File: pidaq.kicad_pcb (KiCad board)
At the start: 2 copper layers, 83.8 x 78.1 mm, 39 parts, among them J1 Screw_Terminal_01x08, J2 Screw_Terminal_01x08, J3 Screw_Terminal_01x10, J4 Screw_Terminal_01x10, J5 Conn_01x02_Male, J6 Conn_01x08_Female, U1 LTC2984CLX-PBF, U2 LTC2418IGN-PBF

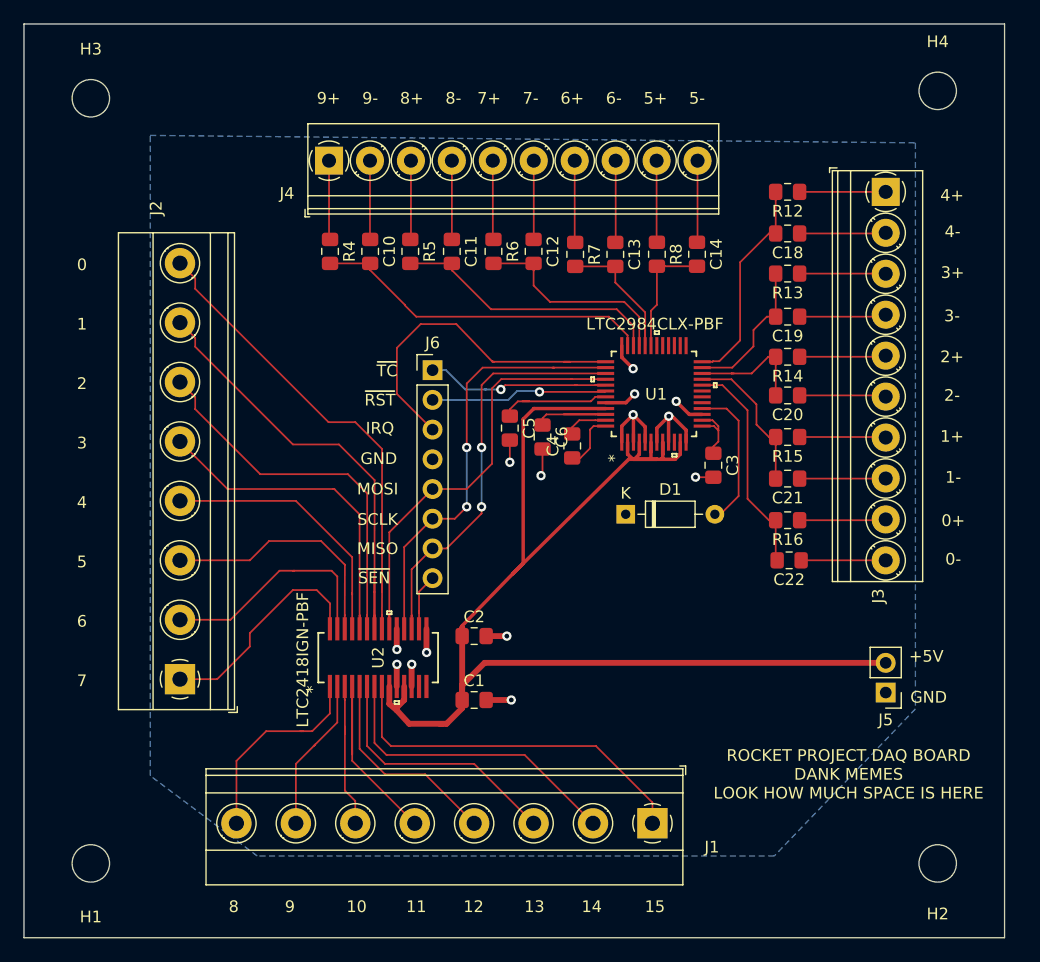
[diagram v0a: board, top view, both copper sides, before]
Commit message: add html preview
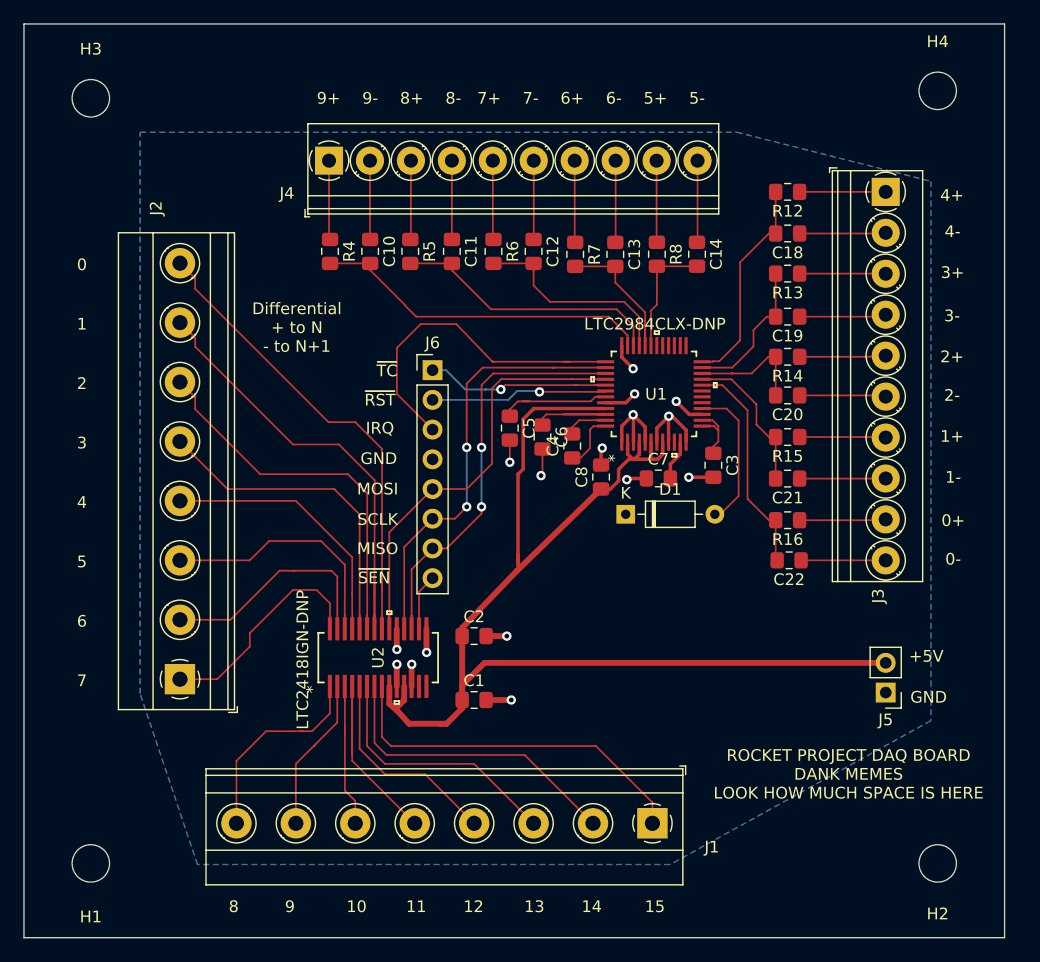
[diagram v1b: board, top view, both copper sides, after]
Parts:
- added C7: 0.1uF, Capacitor_SMD:C_0805_2012Metric_Pad1.15x1.40mm_HandSolder, F.Cu at (131.7, 121.4)
- added C8: 0.1uF, Capacitor_SMD:C_0805_2012Metric_Pad1.15x1.40mm_HandSolder, F.Cu at (126.8, 121.3)
- C10, C11, C12, C13, C14, C18, C19, C20, C21, C22: value C_Small -> 100pF
- C3: value 0.1uF -> 1uF
- C4: value 10uF -> 10uF X7R
- C6: value 10uF -> 10uF X5R
- R12, R13, R14, R15, R16, R4, R5, R6, R7, R8: value R_Small_US -> 100
- U1: value LTC2984CLX-PBF -> LTC2984CLX-DNP
- U2: value LTC2418IGN-PBF -> LTC2418IGN-DNP
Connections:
- U1 pad 11: +5V -> Net-(C7-Pad2)
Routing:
- net +5V: track 113.1 -> 107.2 mm
- net GND: track 112.6 -> 116.4 mm, vias 14 -> 16
- net Net-(C7-Pad2): track 0.00 -> 3.45 mm
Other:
- board text added: "Differential + to N - to N+1"
